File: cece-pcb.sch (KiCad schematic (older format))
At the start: 31 parts, among them J101 SERIAL, J103 Conn_01x03_Male, SW101 SW_Push, SW102 SW_Push, U101 TLV75533PDBV, U102 ESP-12F/ESP07, U103 LM75C

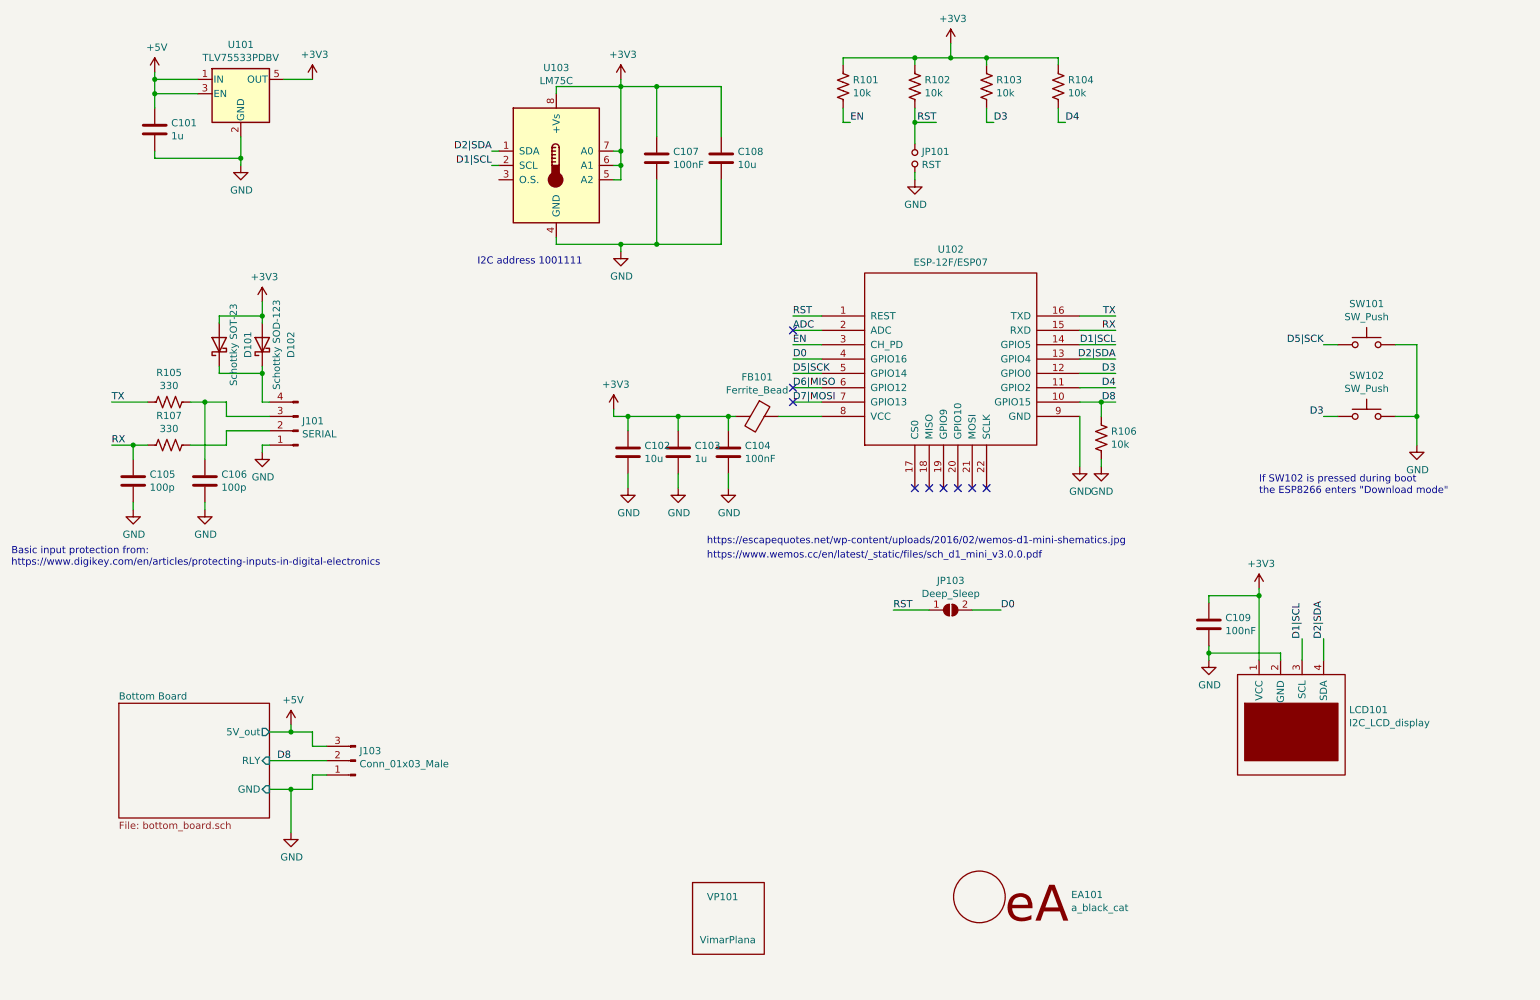
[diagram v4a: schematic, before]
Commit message: Fix minor PCB mistakes and bump up the version to 1.01
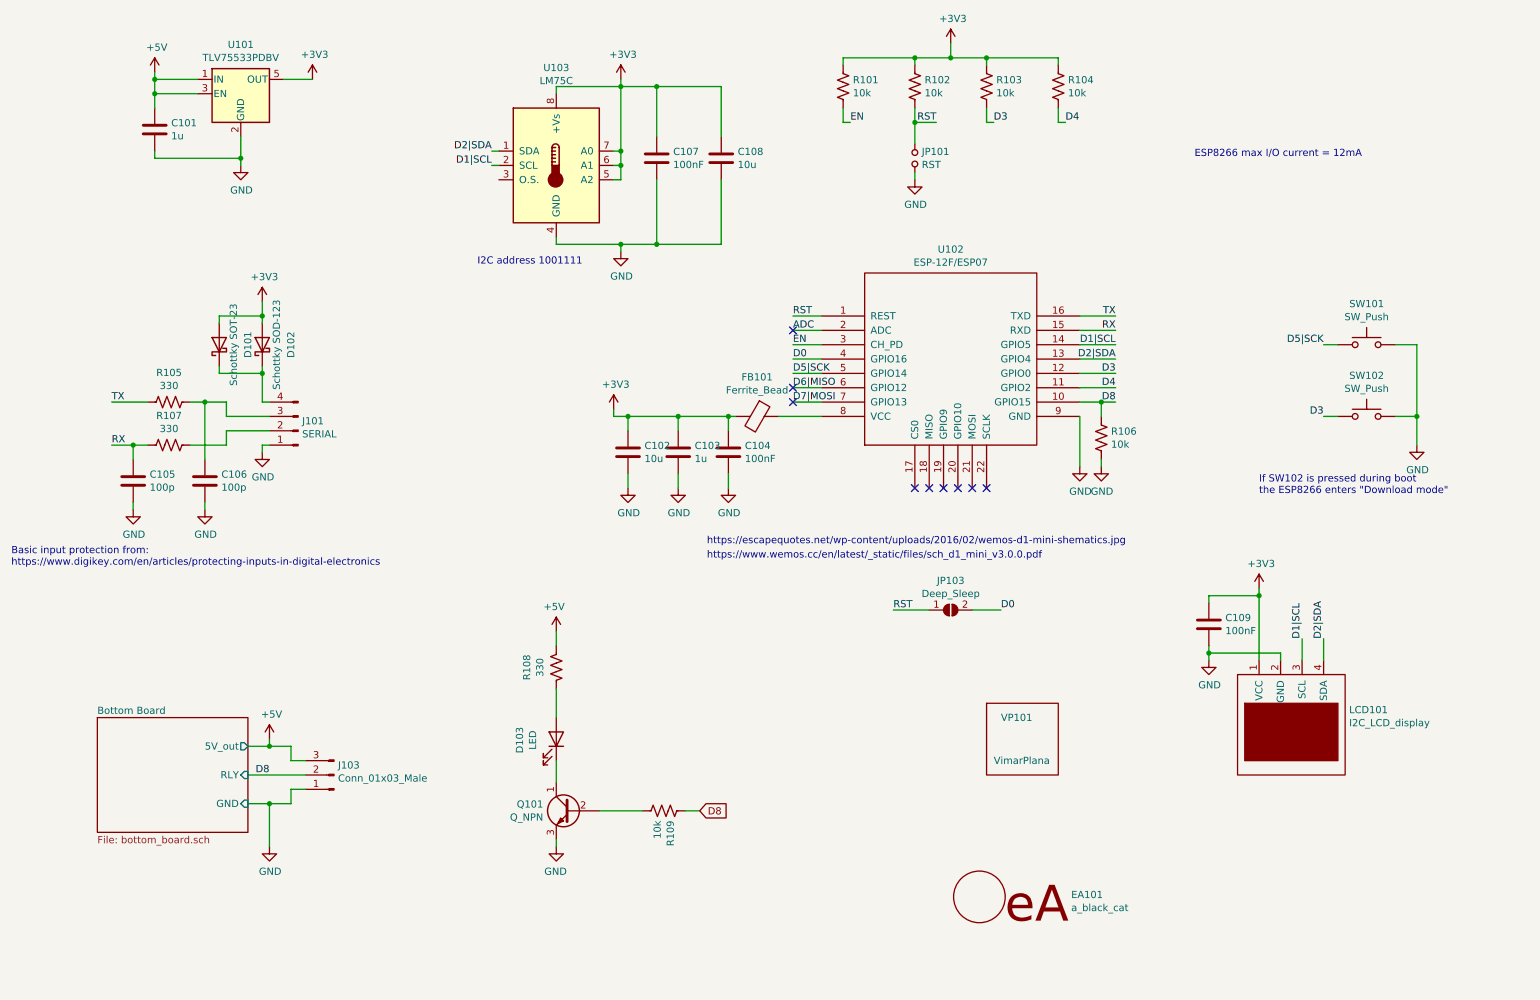
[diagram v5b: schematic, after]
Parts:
- added D103: LED, LED_THT:LED_D3.0mm, symbol Device:LED
- added Q101: Q_NPN, Package_TO_SOT_THT:TO-92L_Inline_Wide, symbol Device:Q_NPN_CBE
- added R108: 330, Resistor_SMD:R_0805_2012Metric_Pad1.15x1.40mm_HandSolder, symbol Device:R_US
- added R109: 10k, Resistor_SMD:R_0805_2012Metric_Pad1.15x1.40mm_HandSolder, symbol Device:R_US
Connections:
- net +5V: now also R108.2
- net D8: now also R109.2
- net GND: now also Q101.3 (E)
- new net: D103.1 (K), Q101.1 (C)
- new net: D103.2 (A), R108.1
- new net: Q101.2 (B), R109.1
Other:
- note added: "ESP8266 max I/O current = 12mA"
- moved on the sheet: J103, VP101
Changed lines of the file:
@@
 L pol:VimarPlana VP101
 U 1 1 60734FBF
-P 5450 7250
-F 0 "VP101" H 5550 7650 50  0000 L CNN
-F 1 "VimarPlana" H 5500 7350 50  0000 L CNN
-F 2 "pol:vimar_plana_3P" H 5450 7250 50  0001 C CNN
-F 3 "" H 5450 7250 50  0001 C CNN
-	1    5450 7250
+P 7500 6000
+F 0 "VP101" H 7600 6400 50  0000 L CNN
+F 1 "VimarPlana" H 7550 6100 50  0000 L CNN
+F 2 "pol:vimar_plana_3P" H 7500 6000 50  0001 C CNN
+F 3 "" H 7500 6000 50  0001 C CNN
+	1    7500 6000
 	1    0    0    -1
 $EndComp
@@
 $EndComp
 $Sheet
-S 1450 5500 1050 800
+S 1300 5600 1050 800
 U 5FC173C3
 F0 "Bottom Board" 50
 F1 "bottom_board.sch" 50
-F2 "GND" I R 2500 6100 50
-F3 "5V_out" O R 2500 5700 50
-F4 "RLY" I R 2500 5900 50
+F2 "GND" I R 2350 6200 50
+F3 "5V_out" O R 2350 5800 50
+F4 "RLY" I R 2350 6000 50
 $EndSheet
 $Comp
@@
 L power:+5V #PWR0118
 U 1 1 60A64392
-P 2650 5650
-F 0 "#PWR0118" H 2650 5500 50  0001 C CNN
-F 1 "+5V" H 2665 5823 50  0000 C CNN
-F 2 "" H 2650 5650 50  0001 C CNN
-F 3 "" H 2650 5650 50  0001 C CNN
-	1    2650 5650
-	1    0    0    -1
-$EndComp
-Wire Wire Line
-	2650 5650 2650 5700
-Wire Wire Line
-	2500 6100 2650 6100
-Wire Wire Line
-	2650 6100 2650 6400
+P 2500 5750
+F 0 "#PWR0118" H 2500 5600 50  0001 C CNN
+F 1 "+5V" H 2515 5923 50  0000 C CNN
+F 2 "" H 2500 5750 50  0001 C CNN
+F 3 "" H 2500 5750 50  0001 C CNN
+	1    2500 5750
+	1    0    0    -1
+$EndComp
+Wire Wire Line
+	2500 5750 2500 5800
+Wire Wire Line
+	2350 6200 2500 6200
+Wire Wire Line
+	2500 6200 2500 6500
 $Comp
 L power:GND #PWR0120
 U 1 1 60A6CA25
-P 2650 6400
-F 0 "#PWR0120" H 2650 6150 50  0001 C CNN
-F 1 "GND" H 2655 6227 50  0000 C CNN
-F 2 "" H 2650 6400 50  0001 C CNN
-F 3 "" H 2650 6400 50  0001 C CNN
-	1    2650 6400
-	1    0    0    -1
-$EndComp
-Text Label 2650 5900 2    50   ~ 0
+P 2500 6500
+F 0 "#PWR0120" H 2500 6250 50  0001 C CNN
+F 1 "GND" H 2505 6327 50  0000 C CNN
+F 2 "" H 2500 6500 50  0001 C CNN
+F 3 "" H 2500 6500 50  0001 C CNN
+	1    2500 6500
+	1    0    0    -1
+$EndComp
+Text Label 2500 6000 2    50   ~ 0
 D8
 NoConn ~ 6150 3400
@@
 L Connector:Conn_01x03_Male J103
 U 1 1 60A91DC5
-P 3100 5900
-F 0 "J103" H 3072 5832 50  0000 R CNN
-F 1 "Conn_01x03_Male" H 3072 5923 50  0000 R CNN
-F 2 "Connector_PinSocket_2.54mm:PinSocket_1x03_P2.54mm_Vertical" H 3100 5900 50  0001 C CNN
-F 3 "~" H 3100 5900 50  0001 C CNN
-	1    3100 5900
+P 2950 6000
+F 0 "J103" H 2922 5932 50  0000 R CNN
+F 1 "Conn_01x03_Male" H 2922 6023 50  0000 R CNN
+F 2 "Connector_PinSocket_2.54mm:PinSocket_1x03_P2.54mm_Vertical" H 2950 6000 50  0001 C CNN
+F 3 "~" H 2950 6000 50  0001 C CNN
+	1    2950 6000
 	-1   0    0    1
 $EndComp
 Wire Wire Line
-	2900 5800 2800 5800
-Wire Wire Line
-	2800 5800 2800 5700
-Wire Wire Line
-	2500 5700 2650 5700
-Connection ~ 2650 5700
-Wire Wire Line
-	2650 5700 2800 5700
-Wire Wire Line
-	2900 6000 2800 6000
-Wire Wire Line
-	2800 6000 2800 6100
-Wire Wire Line
-	2800 6100 2650 6100
-Connection ~ 2650 6100
-Wire Wire Line
-	2500 5900 2900 5900
+	2750 5900 2650 5900
+Wire Wire Line
+	2650 5900 2650 5800
+Wire Wire Line
+	2350 5800 2500 5800
+Connection ~ 2500 5800
+Wire Wire Line
+	2500 5800 2650 5800
+Wire Wire Line
+	2750 6100 2650 6100
+Wire Wire Line
+	2650 6100 2650 6200
+Wire Wire Line
+	2650 6200 2500 6200
+Connection ~ 2500 6200
+Wire Wire Line
+	2350 6000 2750 6000
 $Comp
 L Switch:SW_Push SW101
@@
 Wire Wire Line
 	9050 5150 9550 5150
+Text Notes 8950 1700 0    50   ~ 0
+ESP8266 max I/O current = 12mA
+$Comp
+L Device:LED D103
+U 1 1 60F89700
+P 4500 5750
+AR Path="/60F89700" Ref="D103"  Part="1"
+AR Path="/5FC173C3/60F89700" Ref="D?"  Part="1"
+F 0 "D103" H 4493 5495 50  0000 C CNN
+F 1 "LED" H 4493 5586 50  0000 C CNN
+F 2 "LED_THT:LED_D3.0mm" H 4500 5750 50  0001 C CNN
+F 3 "~" H 4500 5750 50  0001 C CNN
+	1    4500 5750
+	0    1    -1   0
+$EndComp
+$Comp
+L Device:R_US R108
+U 1 1 60F8E1E9
+P 4500 5250
+F 0 "R108" V 4295 5250 50  0000 C CNN
+F 1 "330" V 4386 5250 50  0000 C CNN
+F 2 "Resistor_SMD:R_0805_2012Metric_Pad1.15x1.40mm_HandSolder" V 4540 5240 50  0001 C CNN
+F 3 "~" H 4500 5250 50  0001 C CNN
+	1    4500 5250
+	1    0    0    1
+$EndComp
+$Comp
+L power:+5V #PWR0105
+U 1 1 60F9D4B2
+P 4500 5000
+F 0 "#PWR0105" H 4500 4850 50  0001 C CNN
+F 1 "+5V" H 4515 5173 50  0000 C CNN
+F 2 "" H 4500 5000 50  0001 C CNN
+F 3 "" H 4500 5000 50  0001 C CNN
+	1    4500 5000
+	-1   0    0    -1
+$EndComp
+$Comp
+L Device:Q_NPN_CBE Q101
+U 1 1 60FA106F
+P 4600 6250
+AR Path="/60FA106F" Ref="Q101"  Part="1"
+AR Path="/5FC173C3/60FA106F" Ref="Q?"  Part="1"
+F 0 "Q101" H 4791 6296 50  0000 L CNN
+F 1 "Q_NPN" H 4791 6205 50  0000 L CNN
+F 2 "Package_TO_SOT_THT:TO-92L_Inline_Wide" H 4800 6350 50  0001 C CNN
+F 3 "~" H 4600 6250 50  0001 C CNN
+	1    4600 6250
+	-1   0    0    -1
+$EndComp
+Wire Wire Line
+	4500 5000 4500 5100
+Wire Wire Line
+	4500 5400 4500 5600
+Wire Wire Line
+	4500 5900 4500 6050
+$Comp
+L power:GND #PWR?
+U 1 1 60FB4381
+P 4500 6500
+AR Path="/5FC173C3/60FB4381" Ref="#PWR?"  Part="1"
+AR Path="/60FB4381" Ref="#PWR0124"  Part="1"
+F 0 "#PWR0124" H 4500 6250 50  0001 C CNN
+F 1 "GND" H 4505 6327 50  0000 C CNN
+F 2 "" H 4500 6500 50  0001 C CNN
+F 3 "" H 4500 6500 50  0001 C CNN
+	1    4500 6500
+	-1   0    0    -1
+$EndComp
+Wire Wire Line
+	4500 6500 4500 6450
+$Comp
+L Device:R_US R?
+U 1 1 60FB9946
+P 5250 6250
+AR Path="/5FC173C3/60FB9946" Ref="R?"  Part="1"
+AR Path="/60FB9946" Ref="R109"  Part="1"
+F 0 "R109" H 5182 6204 50  0000 R CNN
+F 1 "10k" H 5182 6295 50  0000 R CNN
+F 2 "Resistor_SMD:R_0805_2012Metric_Pad1.15x1.40mm_HandSolder" V 5290 6240 50  0001 C CNN
+F 3 "~" H 5250 6250 50  0001 C CNN
+	1    5250 6250
+	0    -1   -1   0
+$EndComp
+Wire Wire Line
+	5100 6250 4800 6250
+Wire Wire Line
+	5400 6250 5500 6250
+Text GLabel 5500 6250 2    50   Input ~ 0
+D8
 $EndSCHEMATC

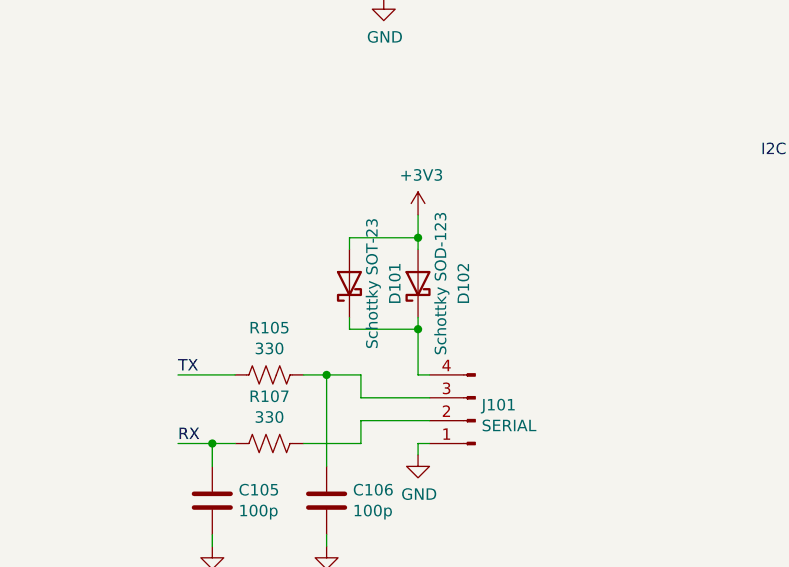
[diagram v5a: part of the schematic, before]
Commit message: Fix diode in the wrong direction and increase PCB revision to 1.02
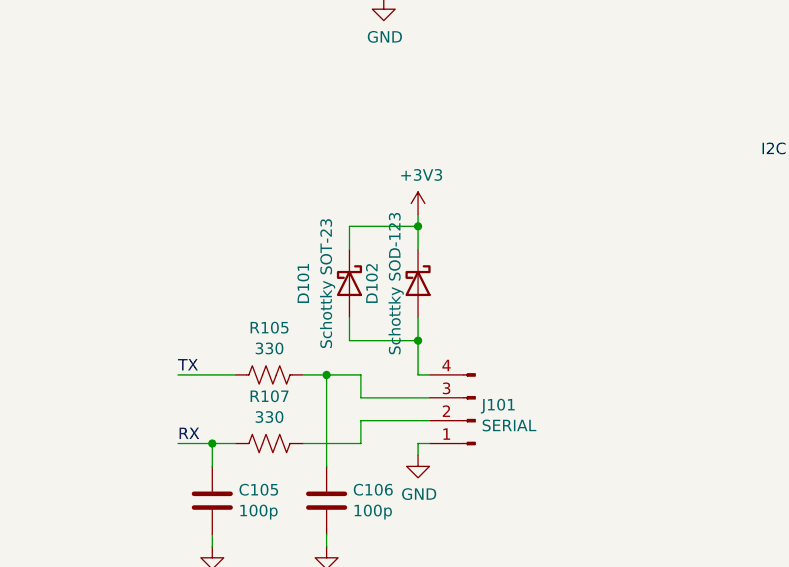
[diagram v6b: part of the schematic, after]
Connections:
- net +3V3: now also D101.1 (K), D102.1 (K); no longer D101.2 (A), D102.2 (A)
- new net: D101.2 (A), D102.2 (A), J101.4 (Pin_4)
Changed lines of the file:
@@
 F 3 "~" H 2150 3000 50  0001 C CNN
 	1    2150 3000
-	0    -1   -1   0
+	0    1    1    0
 $EndComp
 $Comp
@@
 F 3 "~" H 2450 3000 50  0001 C CNN
 	1    2450 3000
-	0    -1   -1   0
+	0    1    1    0
 $EndComp
 $Comp
@@
 Wire Wire Line
 	2500 3400 2450 3400
-Wire Wire Line
-	2450 3400 2450 3200
-Wire Wire Line
-	2150 3150 2150 3200
-Wire Wire Line
-	2150 3200 2450 3200
-Connection ~ 2450 3200
-Wire Wire Line
-	2450 3200 2450 3150
-Wire Wire Line
-	2150 2850 2150 2800
-Wire Wire Line
-	2450 2850 2450 2800
-Wire Wire Line
-	2450 2800 2150 2800
-Wire Wire Line
-	2450 2700 2450 2800
-Connection ~ 2450 2800
 Text Notes 700  4550 0    50   ~ 0
 Basic input protection from:\nhttps://www.digikey.com/en/articles/protecting-inputs-in-digital-electronics
@@
 Text GLabel 5500 6250 2    50   Input ~ 0
 D8
+Wire Wire Line
+	2450 3400 2450 3250
+Wire Wire Line
+	2450 2850 2450 2750
+Wire Wire Line
+	2450 2750 2150 2750
+Wire Wire Line
+	2150 2750 2150 2850
+Connection ~ 2450 2750
+Wire Wire Line
+	2450 2750 2450 2700
+Wire Wire Line
+	2150 3250 2450 3250
+Wire Wire Line
+	2150 3150 2150 3250
+Connection ~ 2450 3250
+Wire Wire Line
+	2450 3250 2450 3150
 $EndSCHEMATC
